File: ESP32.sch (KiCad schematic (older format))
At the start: 60 parts, among them IC1 CP2102N-A02-GQFN28R, J1 NEMA-5-15P-Male, J2 NEMA-5-15R-Female, J3 10118192-0002LF, J4 0.1\" (2.54mm) Headers, K1 G5LE-1, Q1 SS8050, Q2 SS8050, Q3 SS8050, U1 AP2114H-3_3TRG1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

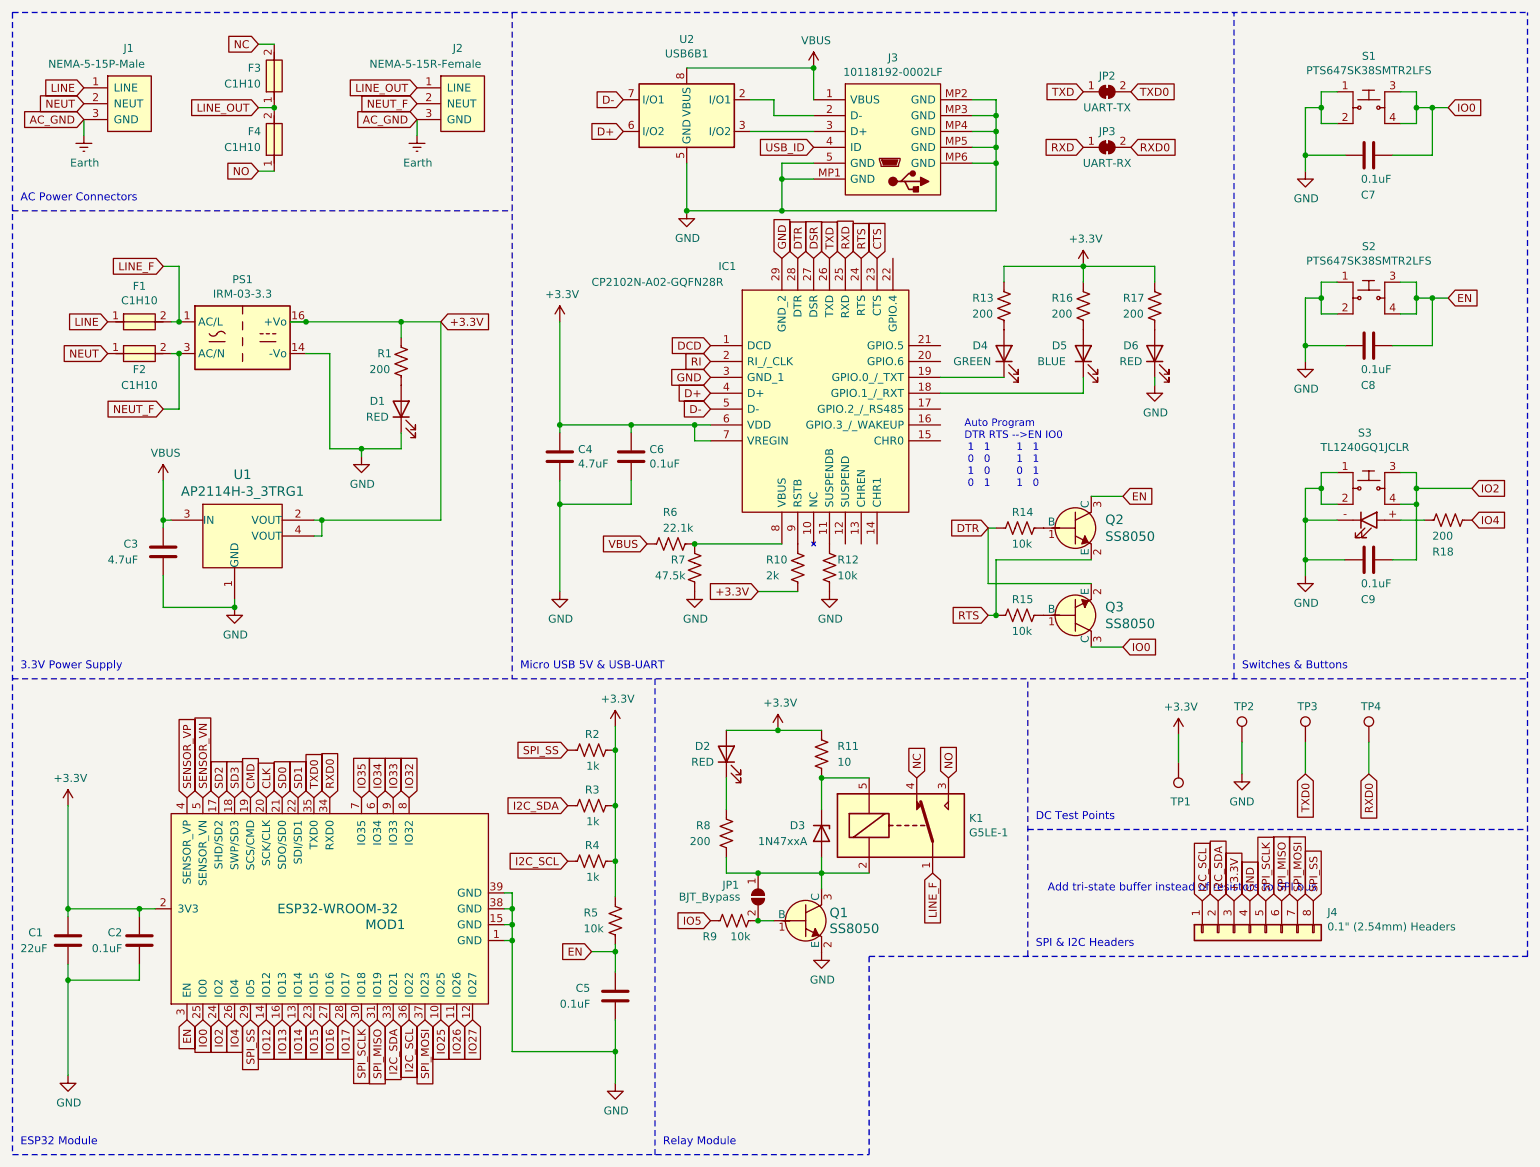
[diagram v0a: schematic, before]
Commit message: Added solder points for connecting relay outputs to NEMA female Line_Out
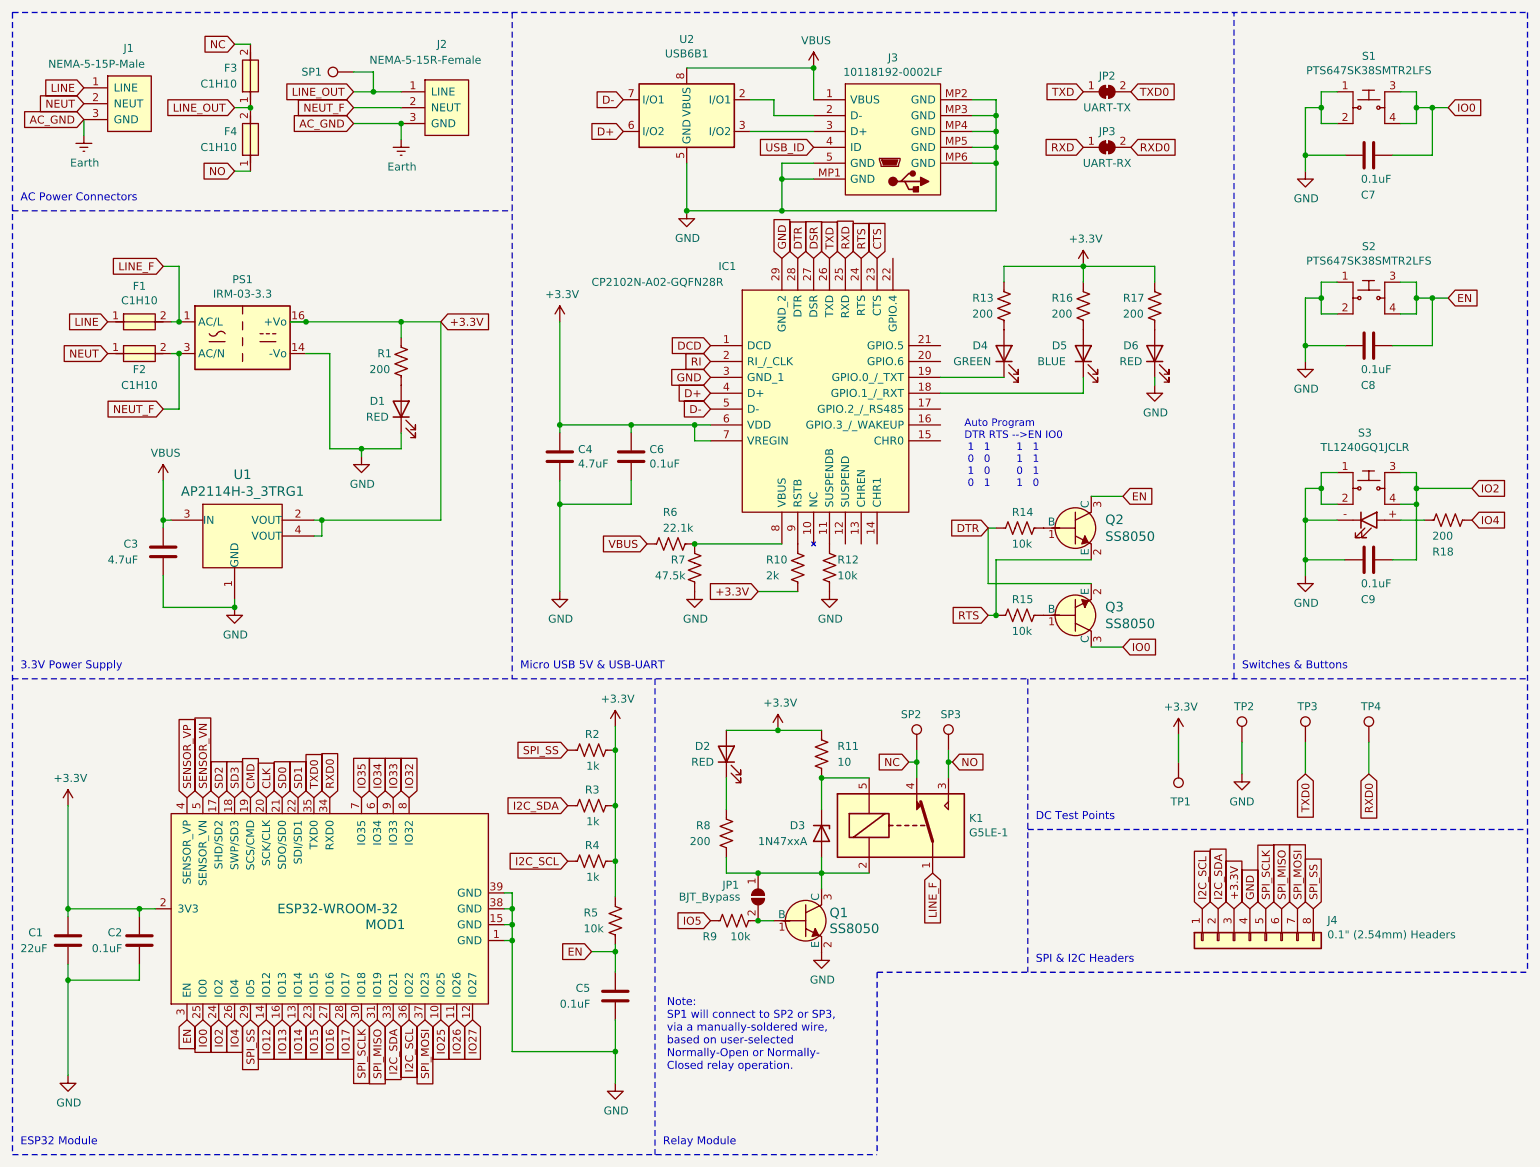
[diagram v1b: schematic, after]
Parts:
- added SP1, SP2, SP3: TestPoint, TestPoint:TestPoint_Plated_Hole_D4.0mm, symbol Connector:TestPoint
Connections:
- net LINE_OUT: now also SP1.1
- net NC: now also SP2.1
- net NO: now also SP3.1
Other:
- note added: "Note: \nSP1 will connect to SP2 or SP3,\nvia a manually-soldered wire,\nbased on user-selected\nNormally-Open or Normally-\nClosed relay operation."
- note removed: "Add tri-state buffer instead of resistors to SPI bus\n"
- moved on the sheet: F3, F4, J2, J4
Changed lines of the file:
@@
 Text GLabel 5150 6375 0    50   Input ~ 0
 IO5
-Text GLabel 6450 5475 1    50   Input ~ 0
+Text GLabel 6400 5375 0    50   Input ~ 0
 NC
-Text GLabel 6650 5475 1    50   Input ~ 0
-NO
 Text GLabel 6550 6075 3    50   Input ~ 0
 LINE_F
@@
 Text GLabel 1200 1225 0    50   Input ~ 0
 NEUT
-Text GLabel 3300 1225 0    50   Input ~ 0
+Text GLabel 2900 1250 0    50   Input ~ 0
 NEUT_F
 Text GLabel 1200 1325 0    50   Input ~ 0
 AC_GND
-Text GLabel 3300 1325 0    50   Input ~ 0
+Text GLabel 2900 1350 0    50   Input ~ 0
 AC_GND
-Text GLabel 3300 1125 0    50   Input ~ 0
-LINE_OUT
 Wire Notes Line
 	750  1900 3900 1900
@@
 	1200 1425 1200 1325
 Wire Wire Line
-	3300 1425 3300 1325
+	3200 1450 3200 1350
 Wire Wire Line
 	1800 2600 1750 2600
@@
 	5450 6375 5550 6375
 Wire Wire Line
-	2300 850  2400 850
-Wire Wire Line
-	2300 1250 2400 1250
-Wire Wire Line
-	2300 1650 2400 1650
-Text GLabel 2300 850  0    50   Input ~ 0
+	2150 850  2250 850
+Wire Wire Line
+	2150 1250 2250 1250
+Wire Wire Line
+	2150 1650 2250 1650
+Text GLabel 2150 850  0    50   Input ~ 0
 NC
-Text GLabel 2300 1250 0    50   Input ~ 0
+Text GLabel 2150 1250 0    50   Input ~ 0
 LINE_OUT
-Text GLabel 2300 1650 0    50   Input ~ 0
+Text GLabel 2150 1650 0    50   Input ~ 0
 NO
-Connection ~ 2400 1250
-Wire Notes Line
-	6150 6600 10300 6600
-Wire Notes Line
-	7150 6600 7150 4850
+Connection ~ 2250 1250
 $Comp
 L Jumper:SolderJumper_2_Open JP1
@@
 L SamacSys_Parts:C1H10 F3
 U 1 1 5FA3943F
-P 2400 1400
-F 0 "F3" V 2800 1525 50  0000 C CNN
-F 1 "C1H10" V 2700 1600 50  0000 C CNN
-F 2 "SamacSys_Parts:FUSC3216X85N" H 2950 1450 50  0001 L CNN
-F 3 "" H 2950 1350 50  0001 L CNN
-F 4 "High Current Rated Fast Acting Chip Fuse" H 2950 1250 50  0001 L CNN "Description"
-F 5 "0.85" H 2950 1150 50  0001 L CNN "Height"
-F 6 "530-C1H10" H 2950 1050 50  0001 L CNN "Mouser Part Number"
-F 7 "https://www.mouser.co.uk/ProductDetail/Bel-Fuse/C1H10?qs=GtFly9OVs8%252BDhtlSiM%2Fykw%3D%3D" H 2950 950 50  0001 L CNN "Mouser Price/Stock"
-F 8 "Stewart Connector" H 2950 850 50  0001 L CNN "Manufacturer_Name"
-F 9 "C1H10" H 2950 750 50  0001 L CNN "Manufacturer_Part_Number"
-	1    2400 1400
+P 2250 1400
+F 0 "F3" V 2650 1525 50  0000 C CNN
+F 1 "C1H10" V 2550 1600 50  0000 C CNN
+F 2 "SamacSys_Parts:FUSC3216X85N" H 2800 1450 50  0001 L CNN
+F 3 "" H 2800 1350 50  0001 L CNN
+F 4 "High Current Rated Fast Acting Chip Fuse" H 2800 1250 50  0001 L CNN "Description"
+F 5 "0.85" H 2800 1150 50  0001 L CNN "Height"
+F 6 "530-C1H10" H 2800 1050 50  0001 L CNN "Mouser Part Number"
+F 7 "https://www.mouser.co.uk/ProductDetail/Bel-Fuse/C1H10?qs=GtFly9OVs8%252BDhtlSiM%2Fykw%3D%3D" H 2800 950 50  0001 L CNN "Mouser Price/Stock"
+F 8 "Stewart Connector" H 2800 850 50  0001 L CNN "Manufacturer_Name"
+F 9 "C1H10" H 2800 750 50  0001 L CNN "Manufacturer_Part_Number"
+	1    2250 1400
 	0    -1   -1   0
 $EndComp
@@
 L power:Earth #PWR07
 U 1 1 5FF0A7F3
-P 3300 1425
-F 0 "#PWR07" H 3300 1175 50  0001 C CNN
-F 1 "Earth" H 3305 1252 50  0000 C CNN
-F 2 "" H 3300 1425 50  0001 C CNN
-F 3 "~" H 3300 1425 50  0001 C CNN
-	1    3300 1425
+P 3200 1450
+F 0 "#PWR07" H 3200 1200 50  0001 C CNN
+F 1 "Earth" H 3205 1277 50  0000 C CNN
+F 2 "" H 3200 1450 50  0001 C CNN
+F 3 "~" H 3200 1450 50  0001 C CNN
+	1    3200 1450
 	1    0    0    -1
 $EndComp
@@
 F 3 "" H 5800 1000 50  0001 C CNN
 	1    5800 1000
-	1    0    0    -1
-$EndComp
-$Comp
-L SamacSys_Parts:NEMA-5-15R-Female J2
-U 1 1 5FE89210
-P 3600 975
-F 0 "J2" H 3525 1075 50  0000 L CNN
-F 1 "NEMA-5-15R-Female" H 3000 975 50  0000 L CNN
-F 2 "SamacSys_Parts:NEMA-5-15R-Female" H 3600 975 50  0001 C CNN
-F 3 "https://www.heyco.com/Power_Components/pdf/Preassembled-Cordset-Components-Female.pdf" H 3600 975 50  0001 C CNN
-	1    3600 975
 	1    0    0    -1
 $EndComp
@@
 L SamacSys_Parts:C1H10 F4
 U 1 1 5FA54D34
-P 2400 1800
-F 0 "F4" V 2800 1925 50  0000 C CNN
-F 1 "C1H10" V 2700 2000 50  0000 C CNN
-F 2 "SamacSys_Parts:FUSC3216X85N" H 2950 1850 50  0001 L CNN
-F 3 "" H 2950 1750 50  0001 L CNN
-F 4 "High Current Rated Fast Acting Chip Fuse" H 2950 1650 50  0001 L CNN "Description"
-F 5 "0.85" H 2950 1550 50  0001 L CNN "Height"
-F 6 "530-C1H10" H 2950 1450 50  0001 L CNN "Mouser Part Number"
-F 7 "https://www.mouser.co.uk/ProductDetail/Bel-Fuse/C1H10?qs=GtFly9OVs8%252BDhtlSiM%2Fykw%3D%3D" H 2950 1350 50  0001 L CNN "Mouser Price/Stock"
-F 8 "Stewart Connector" H 2950 1250 50  0001 L CNN "Manufacturer_Name"
-F 9 "C1H10" H 2950 1150 50  0001 L CNN "Manufacturer_Part_Number"
-	1    2400 1800
+P 2250 1800
+F 0 "F4" V 2650 1925 50  0000 C CNN
+F 1 "C1H10" V 2550 2000 50  0000 C CNN
+F 2 "SamacSys_Parts:FUSC3216X85N" H 2800 1850 50  0001 L CNN
+F 3 "" H 2800 1750 50  0001 L CNN
+F 4 "High Current Rated Fast Acting Chip Fuse" H 2800 1650 50  0001 L CNN "Description"
+F 5 "0.85" H 2800 1550 50  0001 L CNN "Height"
+F 6 "530-C1H10" H 2800 1450 50  0001 L CNN "Mouser Part Number"
+F 7 "https://www.mouser.co.uk/ProductDetail/Bel-Fuse/C1H10?qs=GtFly9OVs8%252BDhtlSiM%2Fykw%3D%3D" H 2800 1350 50  0001 L CNN "Mouser Price/Stock"
+F 8 "Stewart Connector" H 2800 1250 50  0001 L CNN "Manufacturer_Name"
+F 9 "C1H10" H 2800 1150 50  0001 L CNN "Manufacturer_Part_Number"
+	1    2250 1800
 	0    -1   -1   0
 $EndComp
@@
 	-1   0    0    -1
 $EndComp
-Wire Notes Line
-	10300 6600 10300 650
 Connection ~ 7500 2250
 Wire Wire Line
@@
 Wire Notes Line
 	7150 5800 10300 5800
-Text GLabel 8950 6250 1    50   Input ~ 0
+Text GLabel 8950 6300 1    50   Input ~ 0
 SPI_SS
-Text Notes 7200 6550 0    50   ~ 0
+Text Notes 7200 6650 0    50   ~ 0
 SPI & I2C Headers
-Text GLabel 8250 6250 1    50   Input ~ 0
+Text GLabel 8250 6300 1    50   Input ~ 0
 I2C_SCL
-Text GLabel 8350 6250 1    50   Input ~ 0
+Text GLabel 8350 6300 1    50   Input ~ 0
 I2C_SDA
-Text GLabel 8550 6250 1    50   Input ~ 0
+Text GLabel 8550 6300 1    50   Input ~ 0
 GND
-Text GLabel 8650 6250 1    50   Input ~ 0
+Text GLabel 8650 6300 1    50   Input ~ 0
 SPI_SCLK
-Text GLabel 8750 6250 1    50   Input ~ 0
+Text GLabel 8750 6300 1    50   Input ~ 0
 SPI_MISO
-Text GLabel 8850 6250 1    50   Input ~ 0
+Text GLabel 8850 6300 1    50   Input ~ 0
 SPI_MOSI
 $Comp
 L Connector_Generic:Conn_01x08 J4
 U 1 1 5FD421A9
-P 8550 6450
-F 0 "J4" V 8422 5962 50  0000 R CNN
-F 1 "0.1\" (2.54mm) Headers" V 8513 5962 50  0000 R CNN
-F 2 "Connector_PinSocket_2.54mm:PinSocket_1x08_P2.54mm_Vertical" H 8550 6450 50  0001 C CNN
-F 3 "~" H 8550 6450 50  0001 C CNN
-	1    8550 6450
+P 8550 6500
+F 0 "J4" V 8422 6012 50  0000 R CNN
+F 1 "0.1\" (2.54mm) Headers" V 8513 6012 50  0000 R CNN
+F 2 "Connector_PinSocket_2.54mm:PinSocket_1x08_P2.54mm_Vertical" H 8550 6500 50  0001 C CNN
+F 3 "~" H 8550 6500 50  0001 C CNN
+	1    8550 6500
 	0    -1   1    0
 $EndComp
@@
 	1    0    0    -1
 $EndComp
-Text GLabel 8450 6250 1    50   Input ~ 0
+Text GLabel 8450 6300 1    50   Input ~ 0
 +3.3V
 Text GLabel 3050 7000 3    50   Input ~ 0
@@
 Wire Notes Line
 	4800 4850 4800 7850
-Wire Notes Line
-	750  7850 6150 7850
-Wire Notes Line
-	6150 6600 6150 7850
 Wire Wire Line
 	4550 6525 4550 6570
@@
 Wire Wire Line
 	4550 6570 4550 6700
-Text Notes 7275 6200 0    50   ~ 0
-Add tri-state buffer instead of resistors to SPI bus\n
 Wire Wire Line
 	4550 7000 4550 7200
@@
 Wire Notes Line
 	8450 4850 8450 650
+Wire Wire Line
+	6650 5475 6650 5375
+Wire Wire Line
+	6450 5475 6450 5375
+Connection ~ 6650 5375
+Wire Wire Line
+	6650 5375 6650 5300
+Wire Wire Line
+	6400 5375 6450 5375
+Connection ~ 6450 5375
+Wire Wire Line
+	6450 5375 6450 5300
+$Comp
+L SamacSys_Parts:NEMA-5-15R-Female J2
+U 1 1 5FE89210
+P 3500 1000
+F 0 "J2" H 3425 1150 50  0000 L CNN
+F 1 "NEMA-5-15R-Female" H 3000 1050 50  0000 L CNN
+F 2 "SamacSys_Parts:NEMA-5-15R-Female" H 3500 1000 50  0001 C CNN
+F 3 "https://www.heyco.com/Power_Components/pdf/Preassembled-Cordset-Components-Female.pdf" H 3500 1000 50  0001 C CNN
+	1    3500 1000
+	1    0    0    -1
+$EndComp
+Text GLabel 2900 1150 0    50   Input ~ 0
+LINE_OUT
+Wire Wire Line
+	6675 5375 6650 5375
+Text GLabel 6675 5375 2    50   Input ~ 0
+NO
+$Comp
+L Connector:TestPoint SP1
+U 1 1 60055FBD
+P 2900 1025
+F 0 "SP1" V 2900 1225 50  0000 L CNN
+F 1 "TestPoint" H 2750 1275 50  0001 L CNN
+F 2 "TestPoint:TestPoint_Plated_Hole_D4.0mm" H 3100 1025 50  0001 C CNN
+F 3 "~" H 3100 1025 50  0001 C CNN
+	1    2900 1025
+	0    -1   -1   0
+$EndComp
+Wire Wire Line
+	3200 1250 2900 1250
+Wire Wire Line
+	3200 1350 2900 1350
+Connection ~ 3200 1350
+$Comp
+L Connector:TestPoint SP2
+U 1 1 600044FE
+P 6450 5300
+F 0 "SP2" H 6350 5525 50  0000 L CNN
+F 1 "TestPoint" H 6300 5550 50  0001 L CNN
+F 2 "TestPoint:TestPoint_Plated_Hole_D4.0mm" H 6650 5300 50  0001 C CNN
+F 3 "~" H 6650 5300 50  0001 C CNN
+	1    6450 5300
+	1    0    0    -1
+$EndComp
+$Comp
+L Connector:TestPoint SP3
+U 1 1 60004D06
+P 6650 5300
+F 0 "SP3" H 6600 5525 50  0000 L CNN
+F 1 "TestPoint" H 6500 5550 50  0001 L CNN
+F 2 "TestPoint:TestPoint_Plated_Hole_D4.0mm" H 6850 5300 50  0001 C CNN
+F 3 "~" H 6850 5300 50  0001 C CNN
+	1    6650 5300
+	1    0    0    -1
+$EndComp
+Wire Wire Line
+	2900 1150 3025 1150
+Wire Wire Line
+	2900 1025 3025 1025
+Wire Wire Line
+	3025 1025 3025 1150
+Connection ~ 3025 1150
+Wire Wire Line
+	3025 1150 3200 1150
+Text Notes 4875 7325 0    50   ~ 0
+Note: \nSP1 will connect to SP2 or SP3,\nvia a manually-soldered wire,\nbased on user-selected\nNormally-Open or Normally-\nClosed relay operation.
+Wire Notes Line
+	750  7850 6200 7850
+Wire Notes Line
+	6200 6700 10300 6700
+Wire Notes Line
+	10300 650  10300 6700
+Wire Notes Line
+	7150 4850 7150 6700
+Wire Notes Line
+	6200 6700 6200 7850
 $EndSCHEMATC
